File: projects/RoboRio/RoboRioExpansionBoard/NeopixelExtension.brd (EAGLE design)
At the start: 50.5 x 12.7 mm, 6 parts

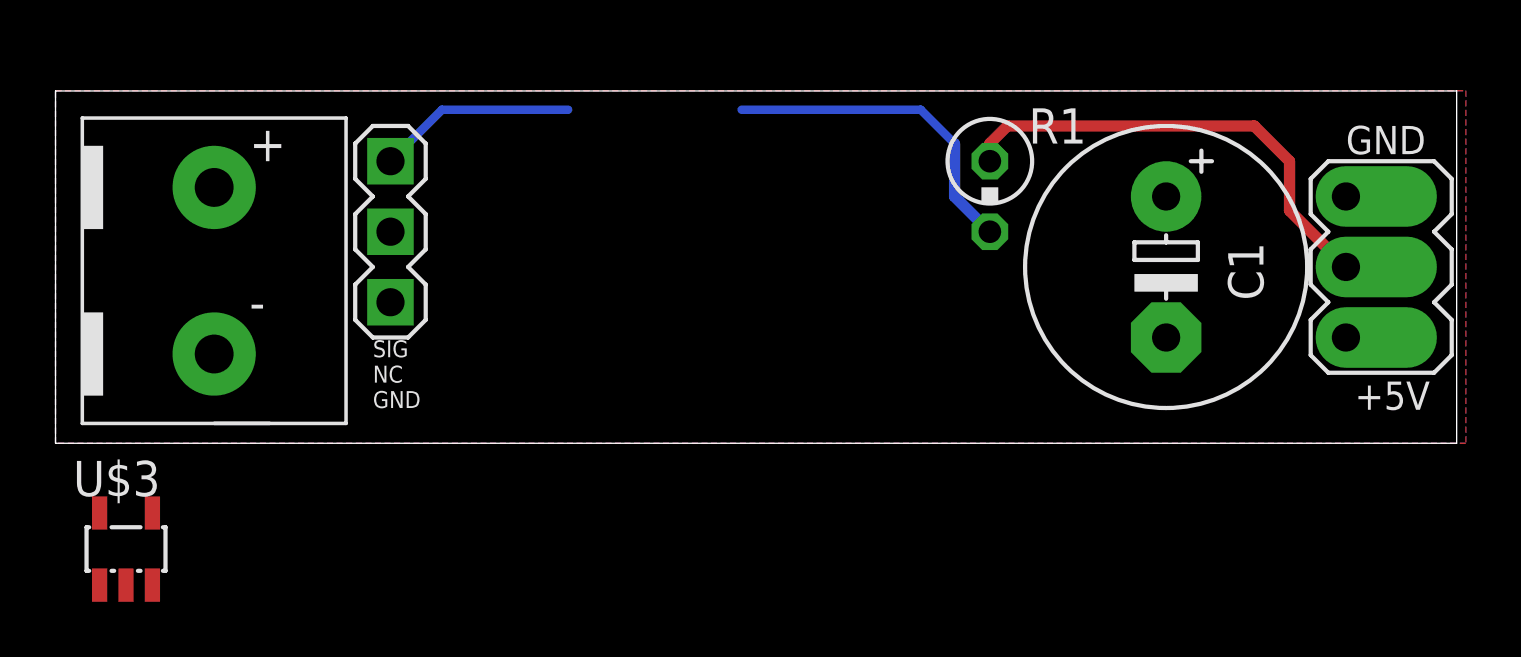
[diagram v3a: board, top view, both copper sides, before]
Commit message: Finished NeopixelRev1
We should probably publish this.
Will work on a rev2 soon
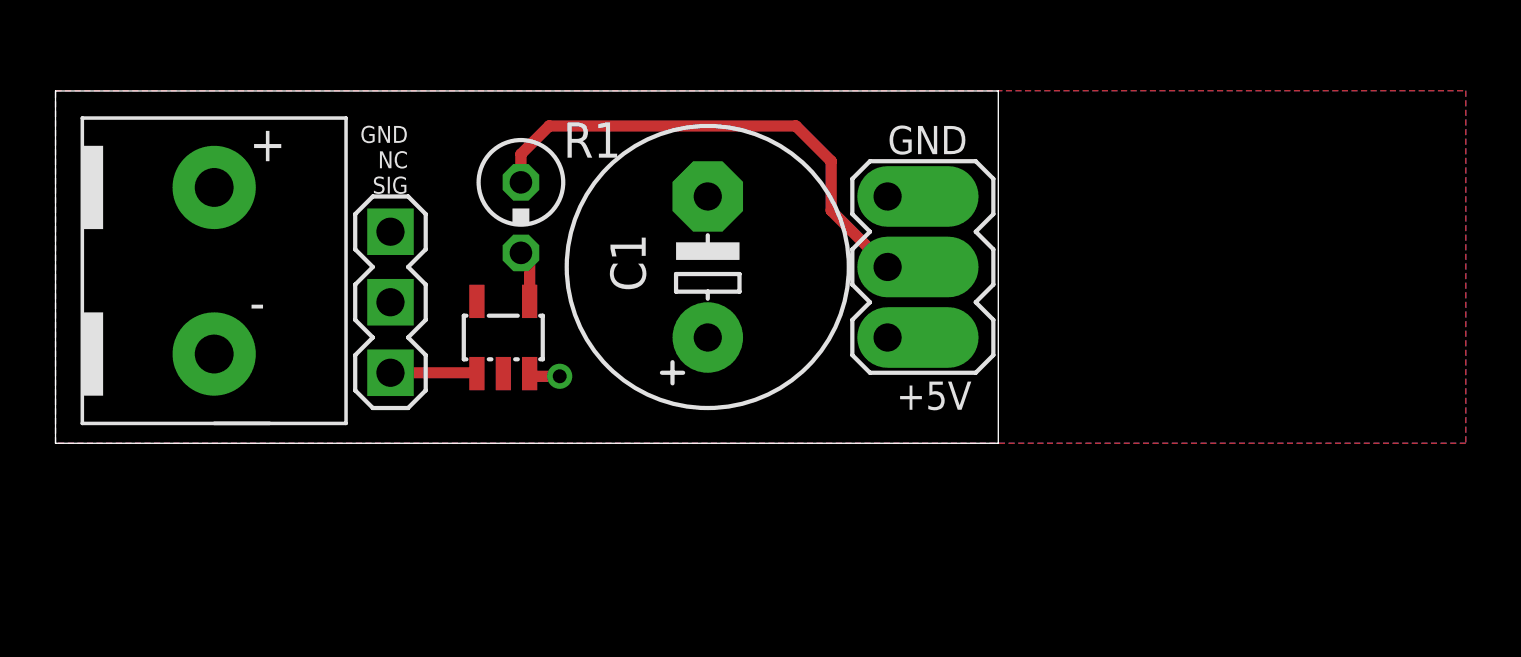
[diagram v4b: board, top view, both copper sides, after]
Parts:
- removed U$3: 74AHCT1G08, SOT25:SOT25
- added S1: 74AHCT1G08, SOT25:SOT25
- moved R1 16.9 mm to (16.8, 8.13)
- moved C1 16.5 mm to (23.5, 6.35), turned to 90 degrees
- moved U$2 16.5 mm to (30.0, 6.35)
- moved IN 2.54 mm to (12.1, 5.08), turned to 270 degrees
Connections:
- net GND: now also S1.3; no longer U$3.3
- net N$3: now also S1.1
- net N$4: now also S1.4; no longer U$3.4
- net VCC: now also S1.2, S1.5; no longer U$3.2, U$3.5
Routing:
- net N$4: track 11.9 -> 1.88 mm
- net N$3: track 7.17 -> 3.14 mm
- net GND: track 0.00 -> 1.12 mm, vias 0 -> 1
- net N$1: track 16.9 -> 17.8 mm
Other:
- board size 50.5 x 12.7 mm -> 34 x 12.7 mm
- board text added: "GND NC SIG"
- board text removed: "SIG NC GND"
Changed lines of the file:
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@@
 <board>
 <plain>
-<wire x1="0" y1="0" x2="50.47" y2="0" width="0" layer="20"/>
-<wire x1="50.47" y1="0" x2="50.47" y2="12.69" width="0" layer="20"/>
-<wire x1="50.47" y1="12.69" x2="0" y2="12.69" width="0" layer="20"/>
+<wire x1="0" y1="0" x2="33.96" y2="0" width="0" layer="20"/>
+<wire x1="33.96" y1="0" x2="33.96" y2="12.69" width="0" layer="20"/>
+<wire x1="33.96" y1="12.69" x2="0" y2="12.69" width="0" layer="20"/>
 <wire x1="0" y1="12.69" x2="0" y2="0" width="0" layer="20"/>
-<text x="11.43" y="1.27" size="0.6096" layer="25">SIG
+<text x="12.7" y="11.43" size="0.6096" layer="25" rot="R180">GND
 NC
-GND</text>
+SIG</text>
 </plain>
 <attributes>
@@
 </autorouter>
 <elements>
-<element name="R1" library="resistor" package="0309V" value="470" x="33.655" y="8.89" smashed="yes" rot="R270">
-<attribute name="NAME" x="35.052" y="10.795" size="1.27" layer="25" ratio="10"/>
-<attribute name="VALUE" x="32.004" y="5.2832" size="1.27" layer="27" ratio="10"/>
-</element>
-<element name="IN" library="con-lstb-modified" package="MA03-1" value="" x="12.065" y="7.62" smashed="yes" rot="R90">
-<attribute name="OC_NEWARK" value="unknown" x="12.065" y="7.62" size="1.778" layer="27" rot="R90" display="off"/>
-<attribute name="MPN" value="" x="12.065" y="7.62" size="1.778" layer="27" rot="R90" display="off"/>
-<attribute name="MF" value="" x="12.065" y="7.62" size="1.778" layer="27" rot="R90" display="off"/>
-<attribute name="OC_FARNELL" value="unknown" x="12.065" y="7.62" size="1.778" layer="27" rot="R90" display="off"/>
-</element>
-<element name="C1" library="adafruit" package="E5-10,5" value="1000uf" x="40.005" y="6.35" smashed="yes" rot="R270">
-<attribute name="NAME" x="42.2402" y="7.239" size="1.27" layer="25" ratio="10" rot="R270"/>
-<attribute name="VALUE" x="36.7792" y="9.4742" size="1.27" layer="27" ratio="10" rot="R270"/>
+<element name="R1" library="resistor" package="0309V" value="470" x="16.764" y="8.128" smashed="yes" rot="R270">
+<attribute name="NAME" x="18.288" y="10.287" size="1.27" layer="25" ratio="10"/>
+<attribute name="VALUE" x="15.1638" y="8.636" size="1.27" layer="27" ratio="10" rot="R90"/>
+</element>
+<element name="IN" library="con-lstb-modified" package="MA03-1" value="" x="12.065" y="5.08" smashed="yes" rot="R270">
+<attribute name="OC_NEWARK" value="unknown" x="12.065" y="5.08" size="1.778" layer="27" rot="R270" display="off"/>
+<attribute name="MPN" value="" x="12.065" y="5.08" size="1.778" layer="27" rot="R270" display="off"/>
+<attribute name="MF" value="" x="12.065" y="5.08" size="1.778" layer="27" rot="R270" display="off"/>
+<attribute name="OC_FARNELL" value="unknown" x="12.065" y="5.08" size="1.778" layer="27" rot="R270" display="off"/>
+</element>
+<element name="C1" library="adafruit" package="E5-10,5" value="1000uf" x="23.495" y="6.35" smashed="yes" rot="R90">
+<attribute name="NAME" x="21.2598" y="5.461" size="1.27" layer="25" ratio="10" rot="R90"/>
+<attribute name="VALUE" x="26.7208" y="3.2258" size="1.27" layer="27" ratio="10" rot="R90"/>
 </element>
 <element name="U$1" library="Molex-39543-0002" package="POWER" value="POWER" x="5.715" y="5.715"/>
-<element name="U$2" library="NeopixelConnector" package="NEODIRECTSOLDERORMA03-1" value="NEOPIXEL1" x="46.482" y="6.35" smashed="yes" rot="R270"/>
-<element name="U$3" library="SOT25" package="SOT25" value="74AHCT1G08" x="2.54" y="-3.81"/>
+<element name="U$2" library="NeopixelConnector" package="NEODIRECTSOLDERORMA03-1" value="NEOPIXEL1" x="29.972" y="6.35" smashed="yes" rot="R270"/>
+<element name="S1" library="SOT25" package="SOT25" value="74AHCT1G08" x="16.129" y="3.81" smashed="yes">
+<attribute name="VALUE" x="13.589" y="1.016" size="0.8128" layer="27"/>
+</element>
 </elements>
 <signals>
@@
 <contactref element="R1" pad="1"/>
 <contactref element="U$2" pad="DATA"/>
-<wire x1="33.655" y1="10.16" x2="33.655" y2="10.795" width="0.4064" layer="1"/>
-<wire x1="33.655" y1="10.795" x2="34.29" y2="11.43" width="0.4064" layer="1"/>
-<wire x1="34.29" y1="11.43" x2="43.18" y2="11.43" width="0.4064" layer="1"/>
-<wire x1="43.18" y1="11.43" x2="44.45" y2="10.16" width="0.4064" layer="1"/>
-<wire x1="44.45" y1="10.16" x2="44.45" y2="8.382" width="0.4064" layer="1"/>
-<wire x1="44.45" y1="8.382" x2="46.482" y2="6.35" width="0.4064" layer="1"/>
+<wire x1="16.764" y1="9.398" x2="16.764" y2="10.414" width="0.4064" layer="1"/>
+<wire x1="16.764" y1="10.414" x2="17.78" y2="11.43" width="0.4064" layer="1"/>
+<wire x1="17.78" y1="11.43" x2="26.67" y2="11.43" width="0.4064" layer="1"/>
+<wire x1="26.67" y1="11.43" x2="27.94" y2="10.16" width="0.4064" layer="1"/>
+<wire x1="27.94" y1="10.16" x2="27.94" y2="8.382" width="0.4064" layer="1"/>
+<wire x1="27.94" y1="8.382" x2="29.972" y2="6.35" width="0.4064" layer="1"/>
 </signal>
 <signal name="GND">
@@
 <contactref element="U$1" pad="GND"/>
 <contactref element="U$2" pad="GND"/>
-<contactref element="U$3" pad="3"/>
-<wire x1="40.005" y1="3.81" x2="46.482" y2="8.89" width="0" layer="19" extent="1-1"/>
-<wire x1="12.065" y1="5.08" x2="40.005" y2="3.81" width="0" layer="19" extent="1-1"/>
-<wire x1="5.715" y1="3.215" x2="12.065" y2="5.08" width="0" layer="19" extent="1-1"/>
-<wire x1="3.49" y1="-5.11" x2="5.715" y2="3.215" width="0" layer="19" extent="1-1"/>
+<contactref element="S1" pad="3"/>
+<via x="18.161" y="2.413" extent="1-16" drill="0.5"/>
+<wire x1="18.161" y1="2.413" x2="17.176" y2="2.413" width="0.4064" layer="1"/>
+<wire x1="17.176" y1="2.413" x2="17.079" y2="2.51" width="0.4064" layer="1"/>
 </signal>
 <signal name="N$3">
 <contactref element="IN" pad="3"/>
-<wire x1="12.065" y1="10.16" x2="13.9192" y2="12.0142" width="0.3048" layer="16"/>
-<wire x1="13.9192" y1="12.0142" x2="18.4658" y2="12.0142" width="0.3048" layer="16"/>
+<contactref element="S1" pad="1"/>
+<wire x1="12.065" y1="2.54" x2="15.179" y2="2.54" width="0.4064" layer="1"/>
+<wire x1="15.179" y1="2.54" x2="15.179" y2="2.51" width="0.4064" layer="1"/>
 </signal>
 <signal name="N$4">
 <contactref element="R1" pad="2"/>
-<wire x1="24.7142" y1="12.0142" x2="31.1658" y2="12.0142" width="0.3048" layer="16"/>
-<wire x1="31.1658" y1="12.0142" x2="32.385" y2="10.795" width="0.3048" layer="16"/>
-<wire x1="32.385" y1="10.795" x2="32.385" y2="8.89" width="0.4064" layer="16"/>
-<wire x1="32.385" y1="8.89" x2="33.655" y2="7.62" width="0.4064" layer="16"/>
-<contactref element="U$3" pad="4"/>
-<wire x1="3.49" y1="-2.51" x2="24.7142" y2="12.0142" width="0" layer="19" extent="1-16"/>
+<contactref element="S1" pad="4"/>
+<wire x1="17.079" y1="5.11" x2="17.079" y2="6.543" width="0.4064" layer="1"/>
+<wire x1="17.079" y1="6.543" x2="16.764" y2="6.858" width="0.4064" layer="1"/>
 </signal>
 <signal name="VCC">
@@
 </polygon>
 <contactref element="U$2" pad="5V"/>
-<contactref element="U$3" pad="5"/>
-<contactref element="U$3" pad="2"/>
-<wire x1="40.005" y1="8.89" x2="46.482" y2="3.81" width="0" layer="19" extent="1-1"/>
-<wire x1="5.715" y1="9.215" x2="40.005" y2="8.89" width="0" layer="19" extent="1-1"/>
-<wire x1="1.59" y1="-2.51" x2="5.715" y2="9.215" width="0" layer="19" extent="1-1"/>
-<wire x1="2.54" y1="-5.11" x2="1.59" y2="-2.51" width="0" layer="19" extent="1-1"/>
+<contactref element="S1" pad="5"/>
+<contactref element="S1" pad="2"/>
 </signal>
 </signals>
